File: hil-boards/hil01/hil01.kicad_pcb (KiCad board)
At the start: 2 copper layers, 61.7 x 30.5 mm, 40 parts, among them J1 USB_C_Receptacle_USB2.0, J2 Conn_01x03_Male, U1 ADUM4160, U2 MAX485E, U3 CH340G, Y1 Crystal

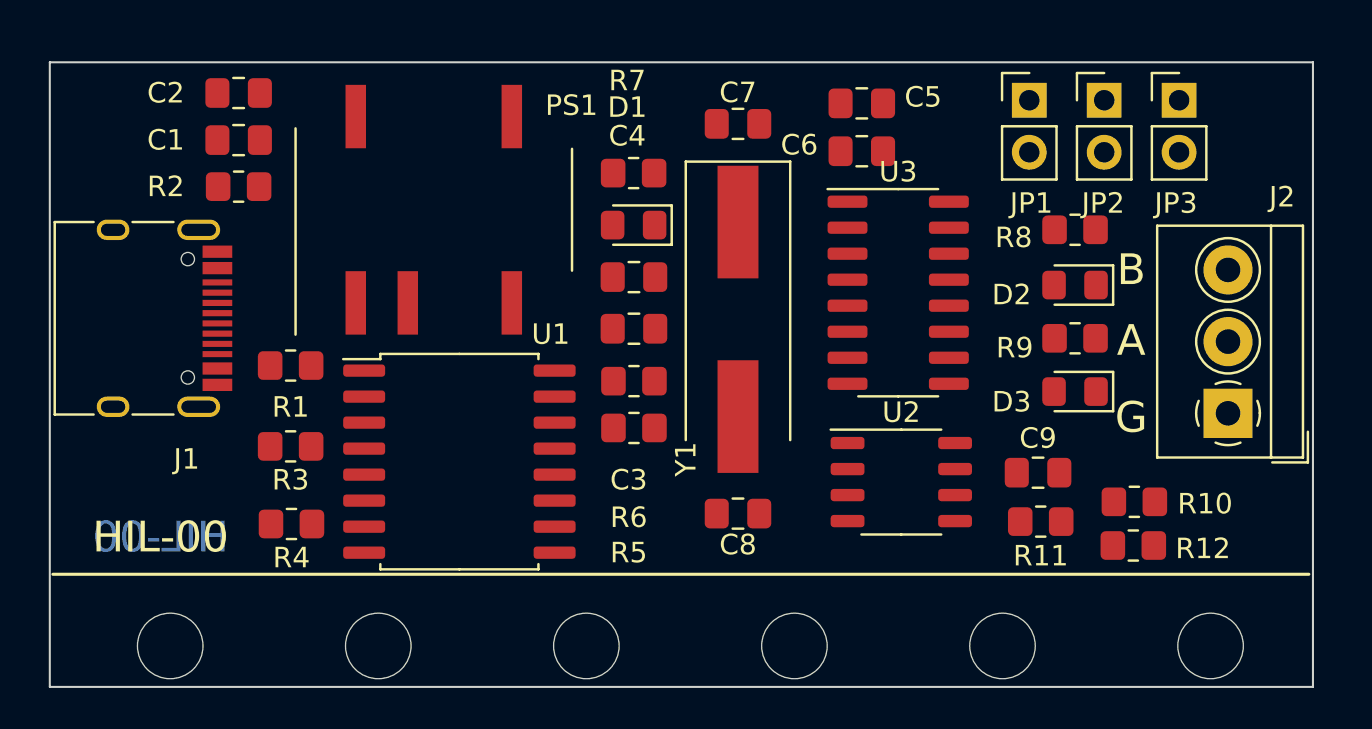
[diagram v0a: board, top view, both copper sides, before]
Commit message: all traces routed
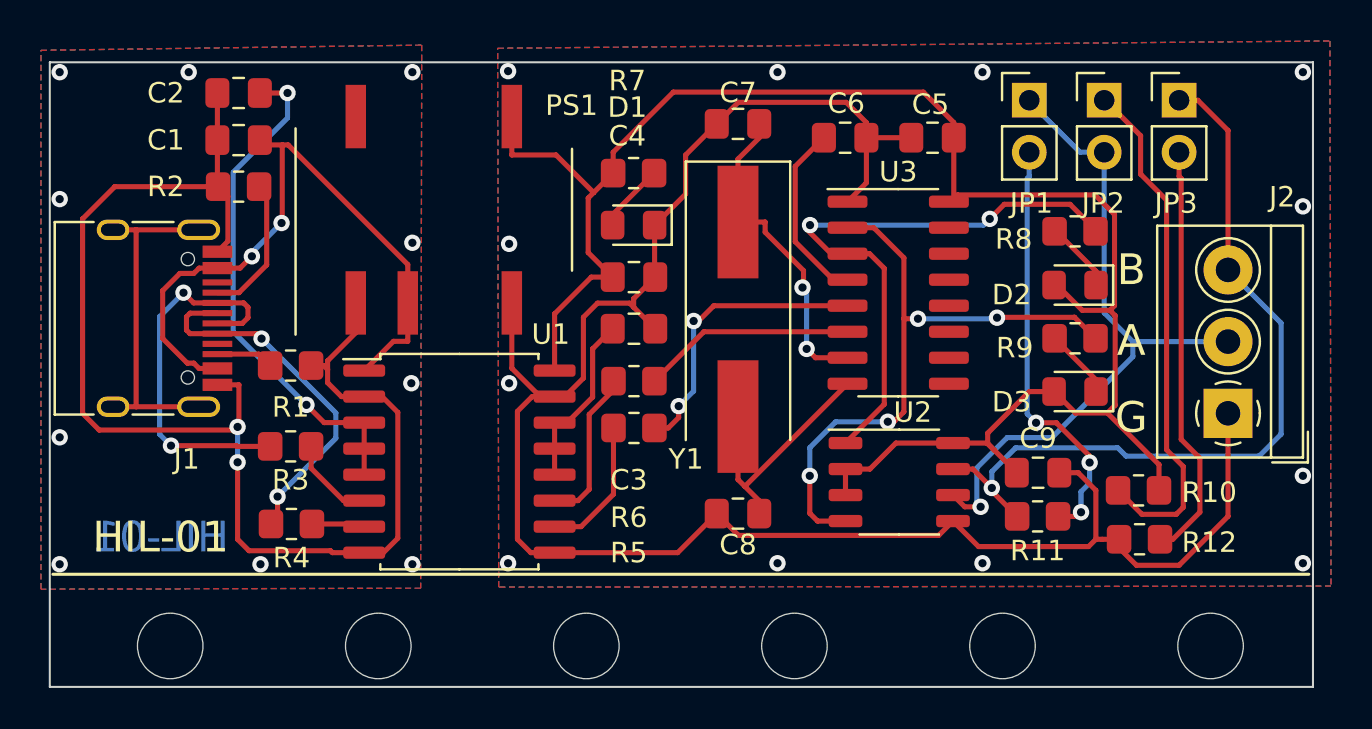
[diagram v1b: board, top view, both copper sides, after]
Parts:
- moved C5 3.84 mm to (143.1, 103.7)
- moved C6 1.05 mm to (138.8, 103.7)
- moved R10 0.59 mm to (153.2, 120.9)
- moved R12 0.43 mm to (153.2, 123.3)
- moved R11 0.30 mm to (148.2, 122.2)
- moved U2 0.10 mm to (141.5, 120.5)
- moved R8 0.08 mm to (150.1, 108.3)
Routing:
- net GND2: track 0.00 -> 96.6 mm, vias 0 -> 12
- net +5V: track 0.00 -> 87.9 mm
- net GND1: track 0.00 -> 65.6 mm, vias 0 -> 12
- net /RS485_B: track 0.00 -> 39.1 mm, vias 0 -> 1
- net /RS485_A: track 0.00 -> 33.4 mm, vias 0 -> 1
- net Net-(C1-Pad1): track 0.00 -> 32.9 mm, vias 0 -> 2
- net /TX: track 0.00 -> 31.1 mm, vias 0 -> 4
- net /RX: track 0.00 -> 29.0 mm, vias 0 -> 2
- net Net-(JP2-Pad1): track 0.00 -> 25.3 mm
- net Net-(C2-Pad1): track 0.00 -> 24.9 mm, vias 0 -> 2
- net Net-(JP1-Pad2): track 0.00 -> 20.8 mm, vias 0 -> 3
- net Net-(JP3-Pad2): track 0.00 -> 20.5 mm
- net Net-(J1-PadA7): track 0.00 -> 18.6 mm, vias 0 -> 2
- net Net-(J1-PadA6): track 0.00 -> 17.9 mm, vias 0 -> 2
- net unconnected-(J1-PadS1): track 0.00 -> 17.0 mm
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- added copper zone on B.Cu, net GND1
- added copper zone on F.Cu, net GND1
- added copper zone on B.Cu, net GND2
- added copper zone on F.Cu, net GND2
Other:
- board text added: "HIL-01"
- board text removed: "HIL-00"
